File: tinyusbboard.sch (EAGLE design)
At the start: 36 parts, among them IC1 MEGA8-AI, Q1 16MHz

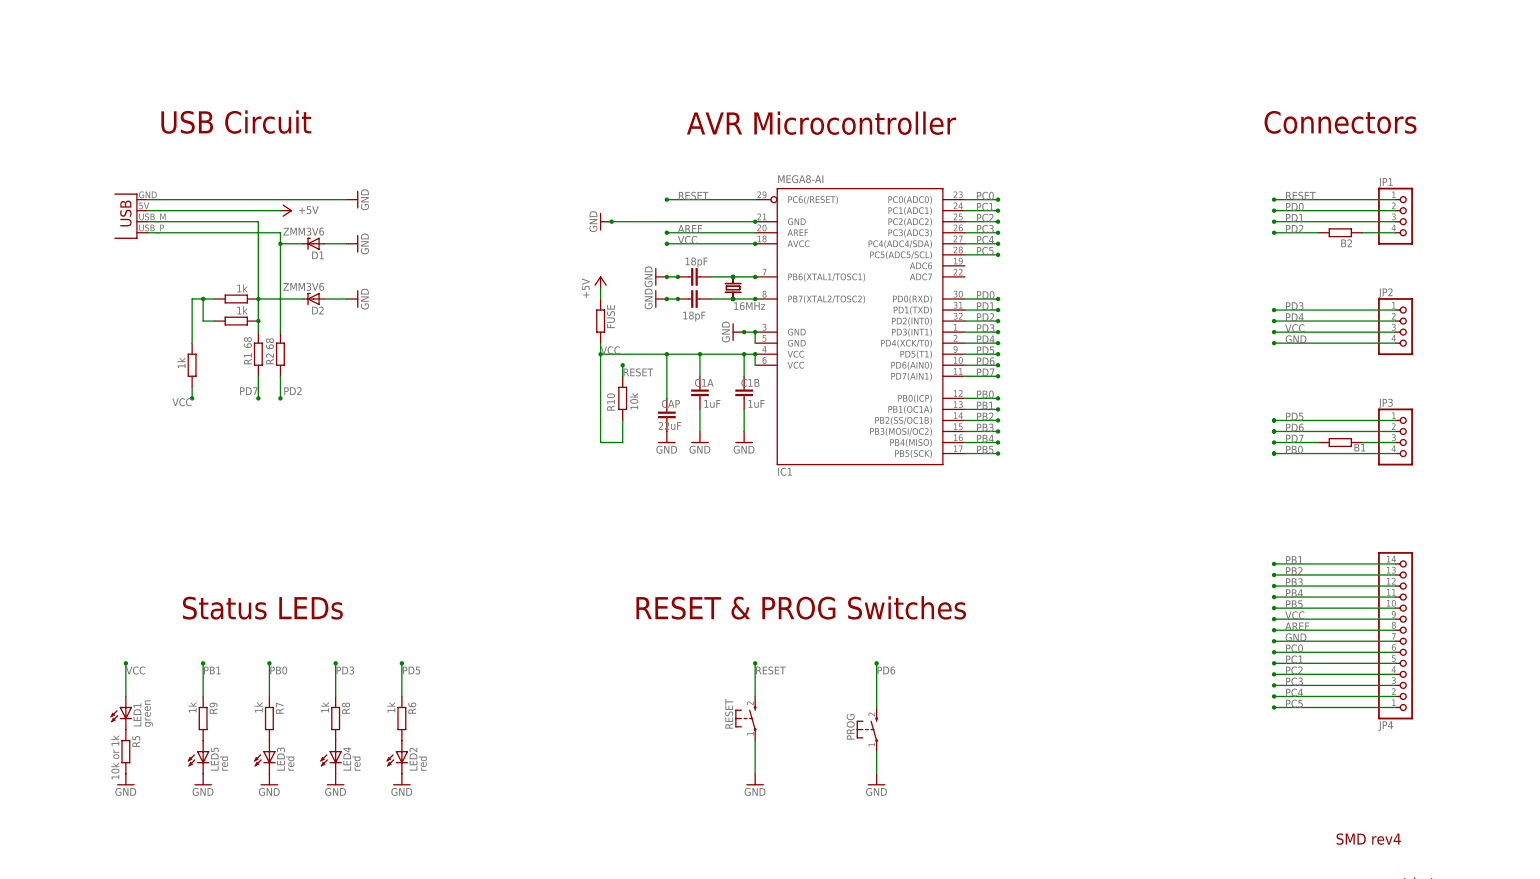
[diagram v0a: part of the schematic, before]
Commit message: More conventional schematic and plus lower capacities to confirm to the USB maximum
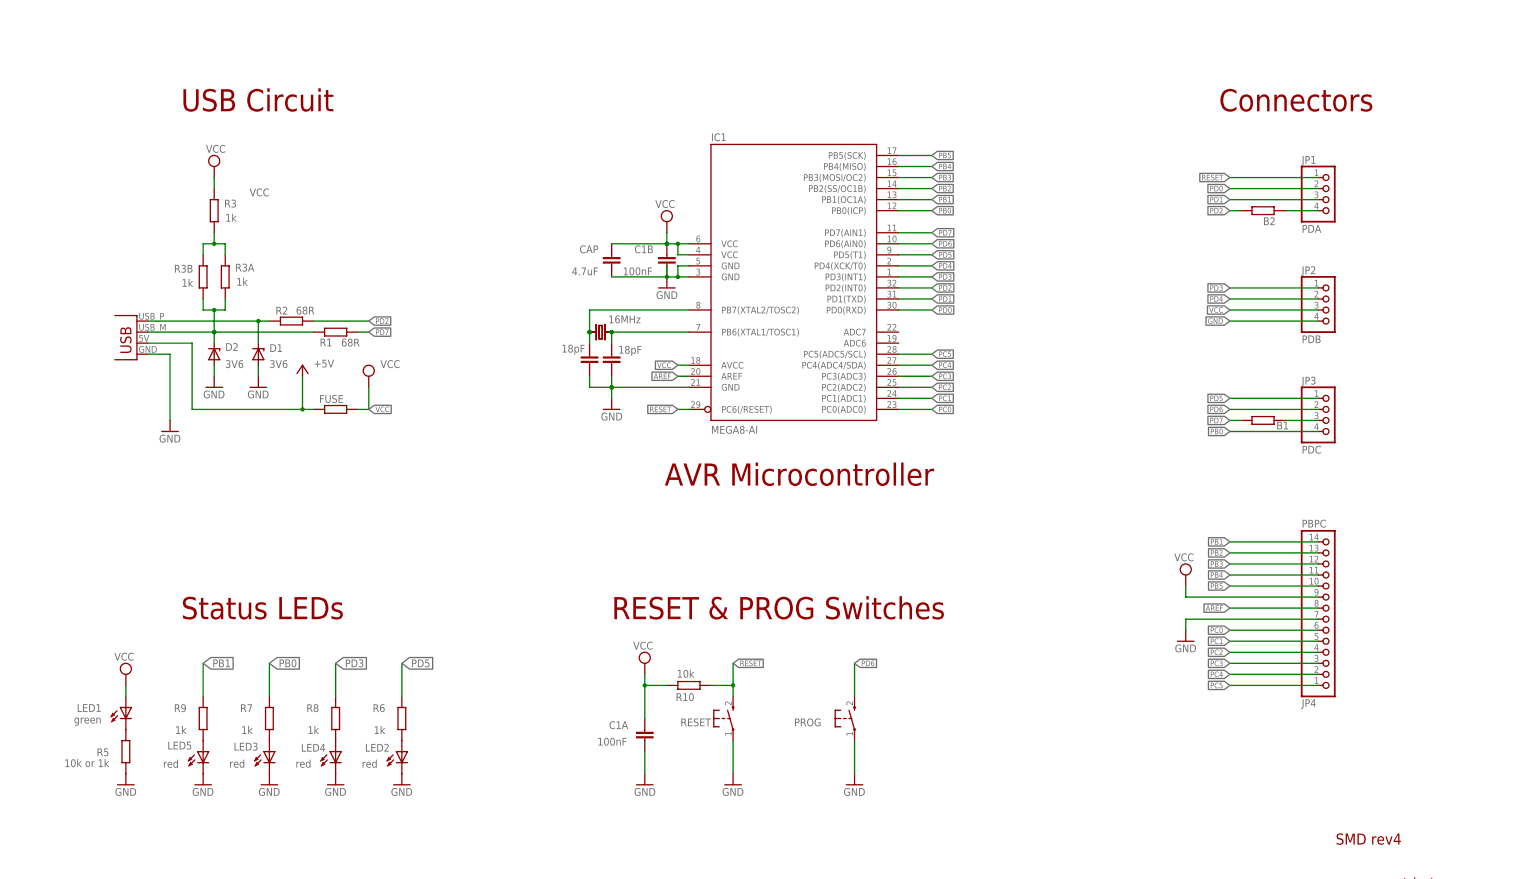
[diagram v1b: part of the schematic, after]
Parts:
- C1A, C1B: value 1uF -> 100nF
- CAP: value 22uF -> 4.7uF
- D1, D2: value ZMM3V6 -> 3V6
- JP1: value (none) -> PDA
- JP2: value (none) -> PDB
- JP3: value (none) -> PDC
- JP4: value (none) -> PBPC
- R1, R2: value 68 -> 68R
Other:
- moved on the sheet: B1, B2, C1A, C1B, CAP, D1, D2, FUSE, IC1, JP1, JP2, JP3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
